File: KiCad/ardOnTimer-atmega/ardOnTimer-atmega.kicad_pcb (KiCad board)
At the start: 2 copper layers, 96.5 x 66 mm, 29 parts, among them J1 FTDI, J2 Power in, K1 KY-019_relay_module, SW1 SW_Push, SW2 SW_Push, SW3 SW_Push, SW4 SW_Push, U1 AMS1117-5.0, U2 ATmega328P-PU, U3 LCD_HD44780, Y1 16MHz

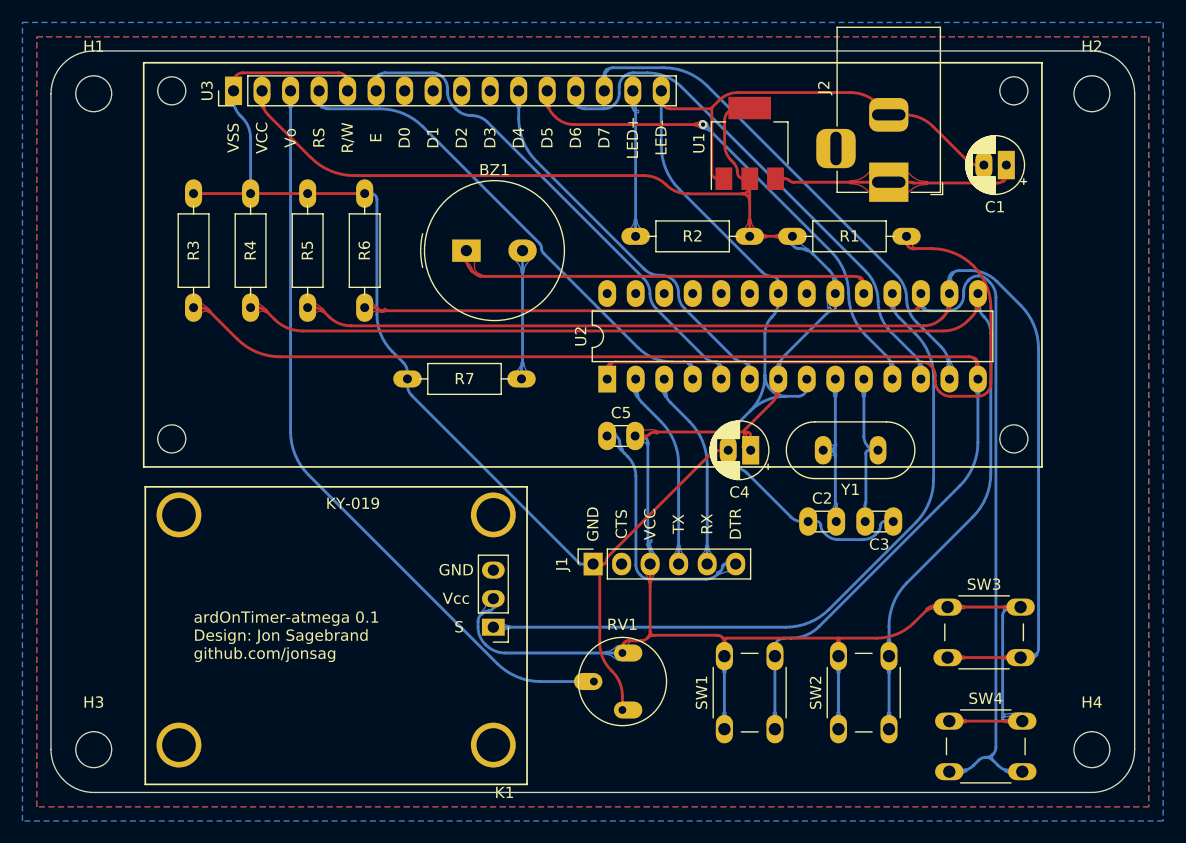
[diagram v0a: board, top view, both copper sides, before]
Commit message: 
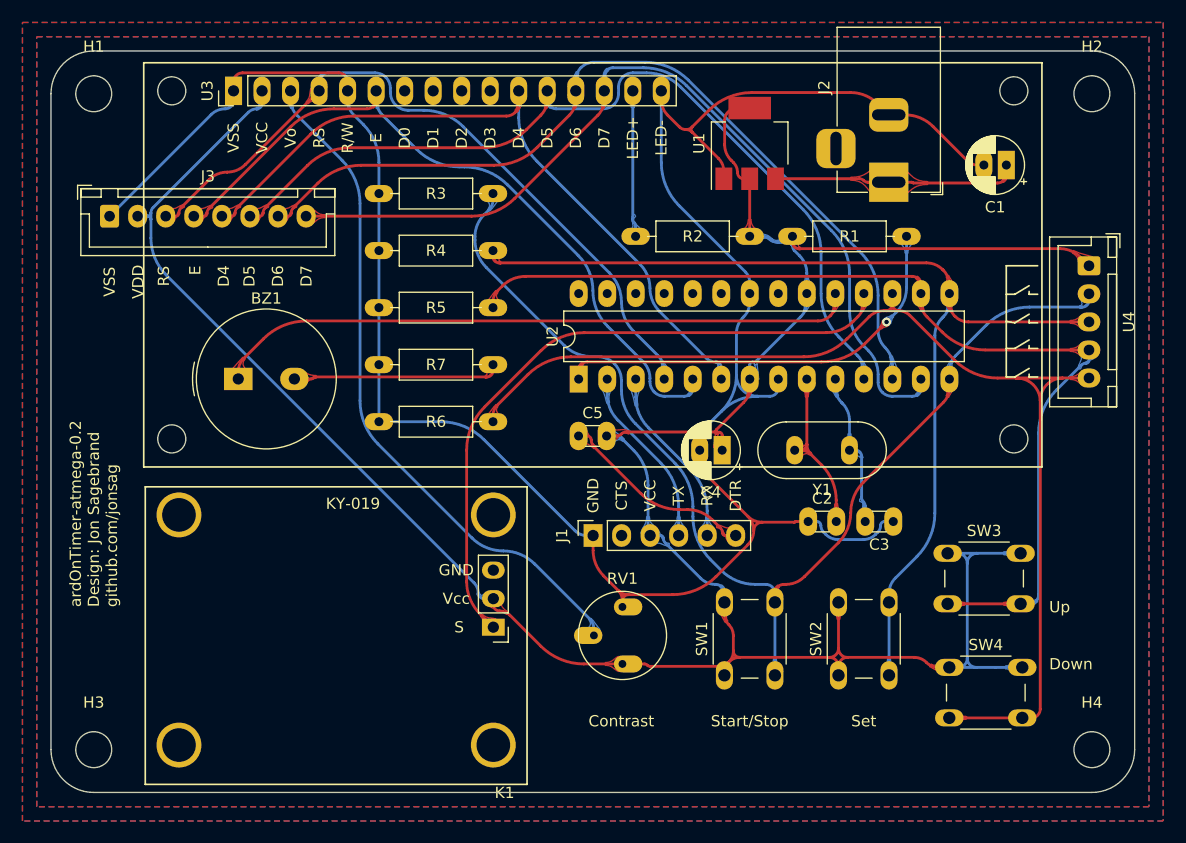
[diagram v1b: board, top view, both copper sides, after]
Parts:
- added J3: 8-pin_header_LCD_interface, My_Headers:8-pin JST LCD, F.Cu at (117.0, 70.6)
- added U4: 5-pin_4_buttons_+_common, My_Headers:5-pin JST 4 buttons + common, F.Cu at (204.2, 75.0)
- R7: value R -> 100R
- moved R3 28.5 mm to (151.1, 68.6), turned to 180 degrees
- moved BZ1 23.3 mm to (128.4, 85.1)
- moved R4 22.2 mm to (151.1, 73.7), turned to 180 degrees
- moved R5 16.5 mm to (151.1, 78.7), turned to 180 degrees
- moved R6 15.3 mm to (151.1, 88.9), turned to 180 degrees
- moved SW1 4.79 mm to (171.7, 111.5)
- moved SW2 4.79 mm to (181.9, 111.5)
- moved SW3 4.79 mm to (191.6, 100.6)
- moved SW4 4.79 mm to (191.8, 110.8)
- moved RV1 4.11 mm to (162.7, 110.5)
- moved R7 2.84 mm to (151.1, 83.8)
- moved C4 2.54 mm to (171.5, 91.4)
- moved U2 2.54 mm to (158.8, 85.1)
- moved J1 2.54 mm to (160.0, 99.0)
- moved C5 2.54 mm to (158.8, 90.2)
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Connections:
- RV1 pad 1: GND -> +5V
- RV1 pad 3: +5V -> GND
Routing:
- net +5V: track 211.5 -> 251.1 mm
- net D5: track 45.0 -> 79.2 mm, vias 1 -> 0
- net D7: track 45.9 -> 79.8 mm
- net D6: track 47.4 -> 77.6 mm
- net D4: track 34.9 -> 64.7 mm
- net D3: track 45.1 -> 64.8 mm
- net D13: track 38.1 -> 57.5 mm
- net D2: track 44.8 -> 64.1 mm
- net Reset: track 56.0 -> 38.0 mm, vias 0 -> 1
- net D10: track 108.2 -> 90.6 mm
- net D9: track 109.8 -> 93.2 mm
- net D8: track 112.6 -> 99.4 mm
- net Net-(BZ1-Pad2): track 11.5 -> 18.6 mm
- net Net-(RV1-Pad2): track 67.4 -> 60.6 mm
- net D11: track 111.0 -> 104.2 mm
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- added copper zone on F.Cu, net (none)
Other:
- board text added: "Contrast"
- board text added: "Down"
- board text added: "Set"
- board text added: "Start/Stop"
- board text added: "Up"
- board text added: "ardOnTimer-atmega-0.2 Design: Jon Sagebrand github.com/jonsag"
- board text removed: "ardOnTimer-atmega 0.1 Design: Jon Sagebrand github.com/jonsag"

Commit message: kicad
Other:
- board text added: "${TITLE}-${REVISION} Design: Jon Sagebrand github.com/jonsag"
- board text removed: "ardOnTimer-atmega-0.2 Design: Jon Sagebrand github.com/jonsag"
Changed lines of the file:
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@@
   )
   (paper "A4")
+  (title_block
+    (title "ardOnTImer-ATmega")
+    (date "2022-09-09")
+    (rev "0.2")
+  )
   (layers
     (0 "F.Cu" signal)
@@
     (effects (font (size 1 1) (thickness 0.15)) (justify left))
   )
-  (gr_text "ardOnTimer-atmega-0.2\nDesign: Jon Sagebrand\ngithub.com/jonsag" (at 115.57 105.41 90) (layer "F.SilkS")
+  (gr_text "${TITLE}-${REVISION}\nDesign: Jon Sagebrand\ngithub.com/jonsag" (at 115.57 105.41 90) (layer "F.SilkS")
     (effects (font (size 1 1) (thickness 0.15)) (justify left))
   )

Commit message: kicad v0.3
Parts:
- removed the C5 at (158.8, 90.2)
- removed the J1 at (160.0, 99.0)
- added C3: 100n, My_Misc:C_Disc_D4.3mm_W1.9mm_P5.00mm_large, F.Cu at (171.5, 92.7)
- added C4: 100n, My_Misc:C_Disc_D4.3mm_W1.9mm_P5.00mm_large, F.Cu at (174.0, 76.2)
- added C7: 100n, My_Misc:C_Disc_D4.3mm_W1.9mm_P5.00mm_large, F.Cu at (198.1, 99.0)
- added J3: FTDI, My_Headers:6-pin FTDI Programmer PinSocket large, F.Cu at (203.2, 99.1)
- added JP1: FTDI Power, My_Parts:Jumper_1x02_P2.54mm_large, F.Cu at (203.2, 91.4)
- moved C2 26.2 mm to (165.1, 66.0), turned to 0 degrees
- moved SW1 3.93 mm to (167.9, 112.5)
- moved SW2 3.93 mm to (178.1, 112.5)
- moved SW4 3.93 mm to (188.0, 111.8)
- moved SW3 3.93 mm to (187.8, 101.6)
- moved Y1 3.93 mm to (186.6, 92.7)
- moved C1 2.54 mm to (194.3, 66.0), turned to 0 degrees
- moved RV1 2.54 mm to (160.1, 110.5)
- moved U4 2.54 mm to (158.8, 87.6)
- moved C6 2.45 mm to (189.2, 97.8)
- moved C5 0.13 mm to (179.1, 97.8)
- renumbered C4 to C2, C2 to C5, C3 to C6, J3 to J1, R2 to R1, R3 to R2, R4 to R3, R5 to R4, R6 to R5, R7 to R6, R1 to R7, U3 to U1, U4 to U2, U1 to U3, U2 to U4
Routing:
- net D0/Rx: track 16.1 -> 52.2 mm
- net D1/Tx: track 16.1 -> 49.0 mm
- net Net-(C5-Pad1): track 17.6 -> 0.00 mm
- net Reset: track 38.0 -> 53.8 mm, vias 1 -> 0
- net Net-(C7-Pad1): track 0.00 -> 14.8 mm
- net Net-(J3-Pad3): track 0.00 -> 14.2 mm
- net D8: track 99.4 -> 110.0 mm
- net D12: track 59.2 -> 51.1 mm
- net +5V: track 251.1 -> 244.4 mm
- net D9: track 93.2 -> 98.2 mm
- net XTAL1: track 15.9 -> 11.4 mm
- net VCC: track 21.9 -> 18.5 mm
- net D2: track 64.1 -> 67.5 mm
- net D10: track 90.6 -> 93.8 mm
- net D7: track 79.8 -> 76.7 mm
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- removed copper zone on B.Cu, net GND
- removed copper zone on F.Cu, net GND
